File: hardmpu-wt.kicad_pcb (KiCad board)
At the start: 2 copper layers, 106 x 95.3 mm, 49 parts, among them J1 MIDI, J2 User, J3 LineOut, J4 ISP, J5 JTAG, J6 Wavetable, J7 AuxOut, J8 XT Bus, U1 74HCT138, U10 78L05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

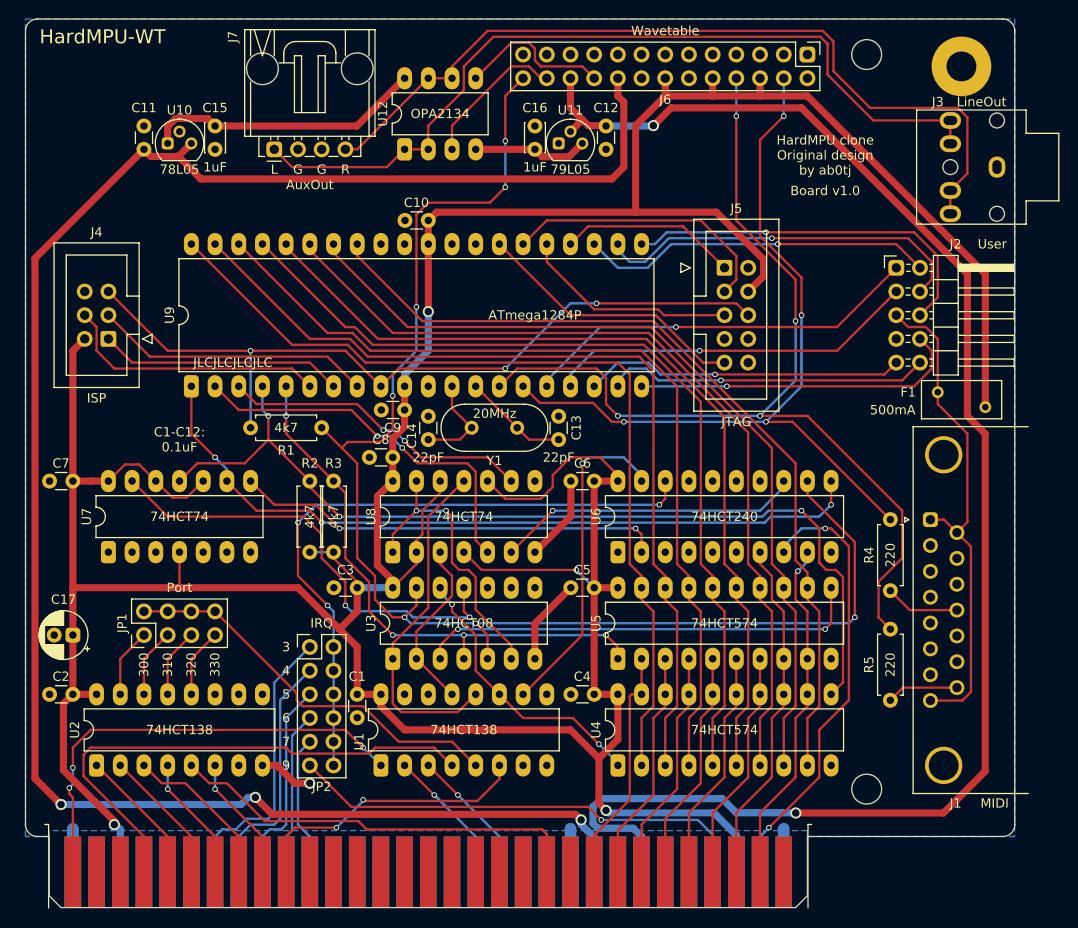
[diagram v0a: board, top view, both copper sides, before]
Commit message: Tweak component values
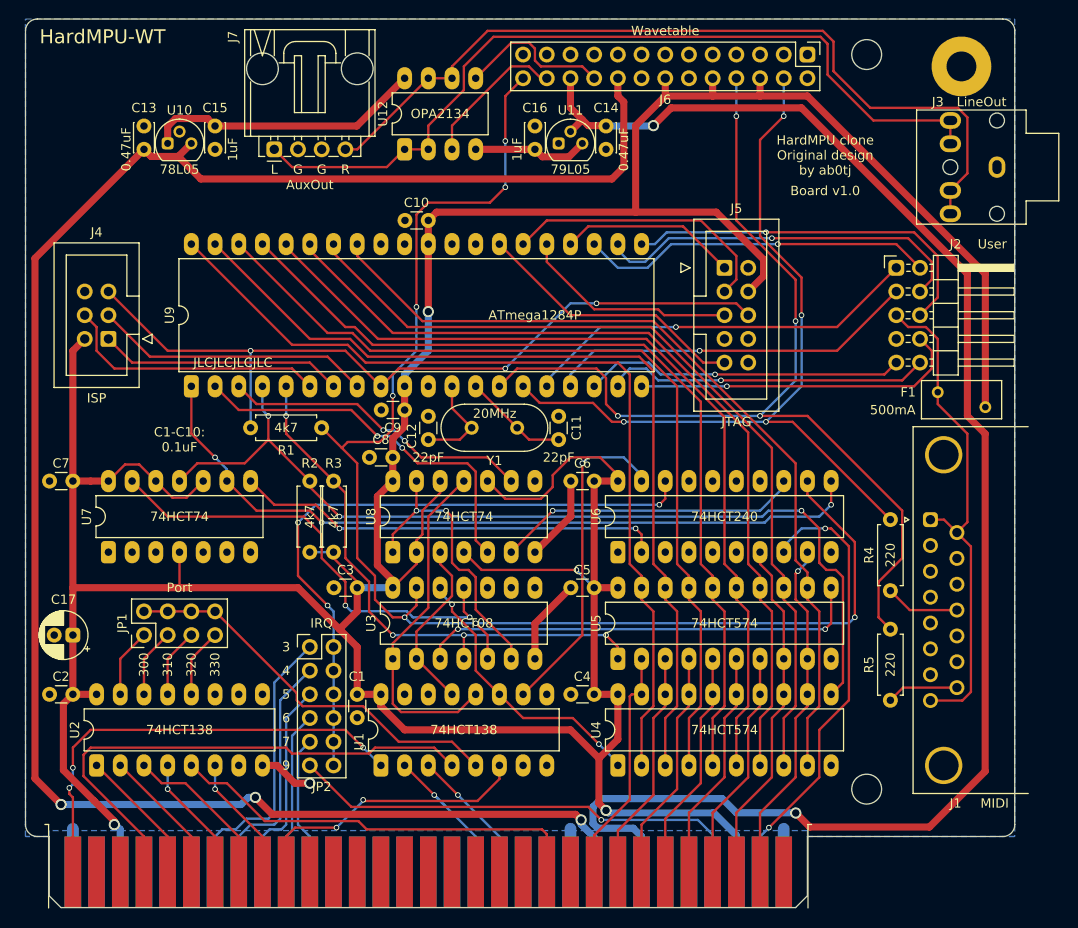
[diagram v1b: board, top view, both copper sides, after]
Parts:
- removed the C11 at (96.5, 67.3)
- removed the C12 at (146.1, 67.3)
- added C13: 0.47uF, Capacitor_THT:C_Disc_D3.0mm_W2.0mm_P2.50mm, F.Cu at (96.5, 67.3)
- added C14: 0.47uF, Capacitor_THT:C_Disc_D3.0mm_W2.0mm_P2.50mm, F.Cu at (146.1, 67.3)
- renumbered C13 to C11, C14 to C12
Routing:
- net -12V: track 166.9 -> 168.1 mm
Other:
- board text added: "C1-C10: 0.1uF"
- board text removed: "C1-C12: 0.1uF"

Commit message: Move DA-15 so board aligns with Keystone 9200-11 bracket
Adapt board to fit common Keystone 9200-11, add jumpers to switch wavetable between Internal and External UART
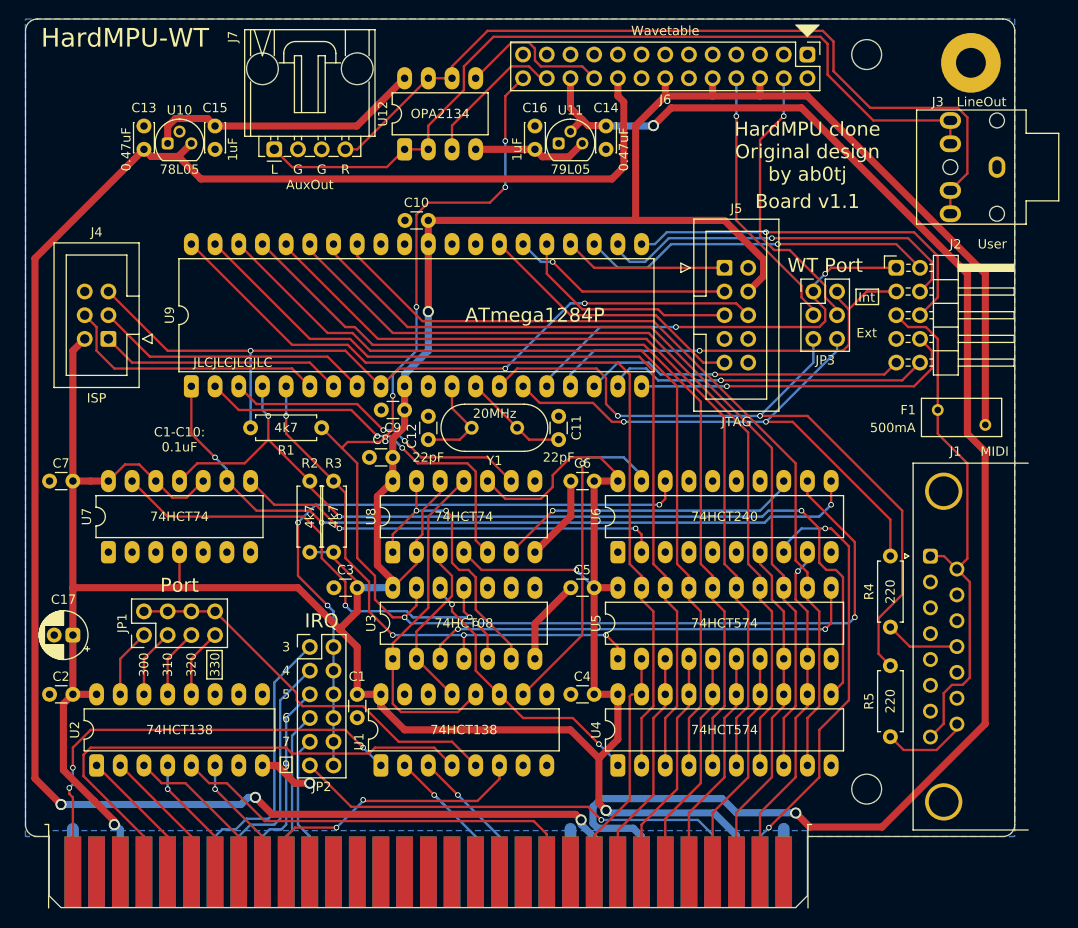
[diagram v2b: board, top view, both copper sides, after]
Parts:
- added JP3: WT Port, Connector_PinHeader_2.54mm:PinHeader_2x03_P2.54mm_Vertical, F.Cu at (168.3, 82.5)
- H1: value WT_Hole1 -> WT_Hole
- H2: value WT_Hole2 -> WT_Hole
- moved J1 3.91 mm to (180.8, 110.9)
- moved R5 3.91 mm to (176.5, 130.3)
- moved R4 3.91 mm to (176.5, 118.5)
- moved F1 1.91 mm to (181.6, 95.2)
- moved H3 1.09 mm to (185.2, 58.0)
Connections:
- J2 pad 1: /USER0 -> /RX1
- J2 pad 10: /USER3 -> /USER1
- J2 pad 3: /USER1 -> /TX1
- J2 pad 6: /USER5 -> /USER3
- J2 pad 8: /USER4 -> /USER2
- J2 pad 9: /USER2 -> /USER0
- J6 pad 4: MIDI_TX -> WT_TX
- J6 pad 8: MIDI_RX -> WT_RX
- R4 pad 2: MIDI_TX -> /TX0
- R5 pad 2: MIDI_RX -> /RX0
- U9 pad 14: MIDI_RX -> /RX0
- U9 pad 15: MIDI_TX -> /TX0
- U9 pad 16: /USER0 -> /RX1
- U9 pad 17: /USER1 -> /TX1
- U9 pad 18: /USER2 -> /USER0
- U9 pad 19: /USER3 -> /USER1
- U9 pad 20: /USER4 -> /USER2
- U9 pad 21: /USER5 -> /USER3
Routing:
- net MIDI_RX: track 106.6 -> 0.00 mm, vias 4 -> 0
- net MIDI_TX: track 86.6 -> 0.00 mm, vias 4 -> 0
- net /RX0: track 0.00 -> 80.7 mm, vias 0 -> 2
- net /TX0: track 0.00 -> 61.2 mm, vias 0 -> 2
- net /RX1: track 0.00 -> 47.1 mm, vias 0 -> 2
- net /TX1: track 0.00 -> 44.5 mm, vias 0 -> 1
- net /USER5: track 40.5 -> 0.00 mm, vias 1 -> 0
- net /USER4: track 35.6 -> 0.00 mm, vias 1 -> 0
- net WT_TX: track 0.00 -> 30.8 mm, vias 0 -> 1
- net WT_RX: track 0.00 -> 28.8 mm, vias 0 -> 1
- net /USER0: track 43.1 -> 34.5 mm
- net /TDO: track 29.8 -> 23.7 mm, vias 0 -> 1
- net /USER3: track 34.9 -> 40.5 mm
- net /USER1: track 39.9 -> 34.9 mm
- net -12V: track 168.1 -> 165.2 mm
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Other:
- board text added: "Board v1.1"
- board text added: "Ext"
- board text added: "Int"
- board text removed: "Board v1.0"

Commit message: Migrate project to KiCad 6
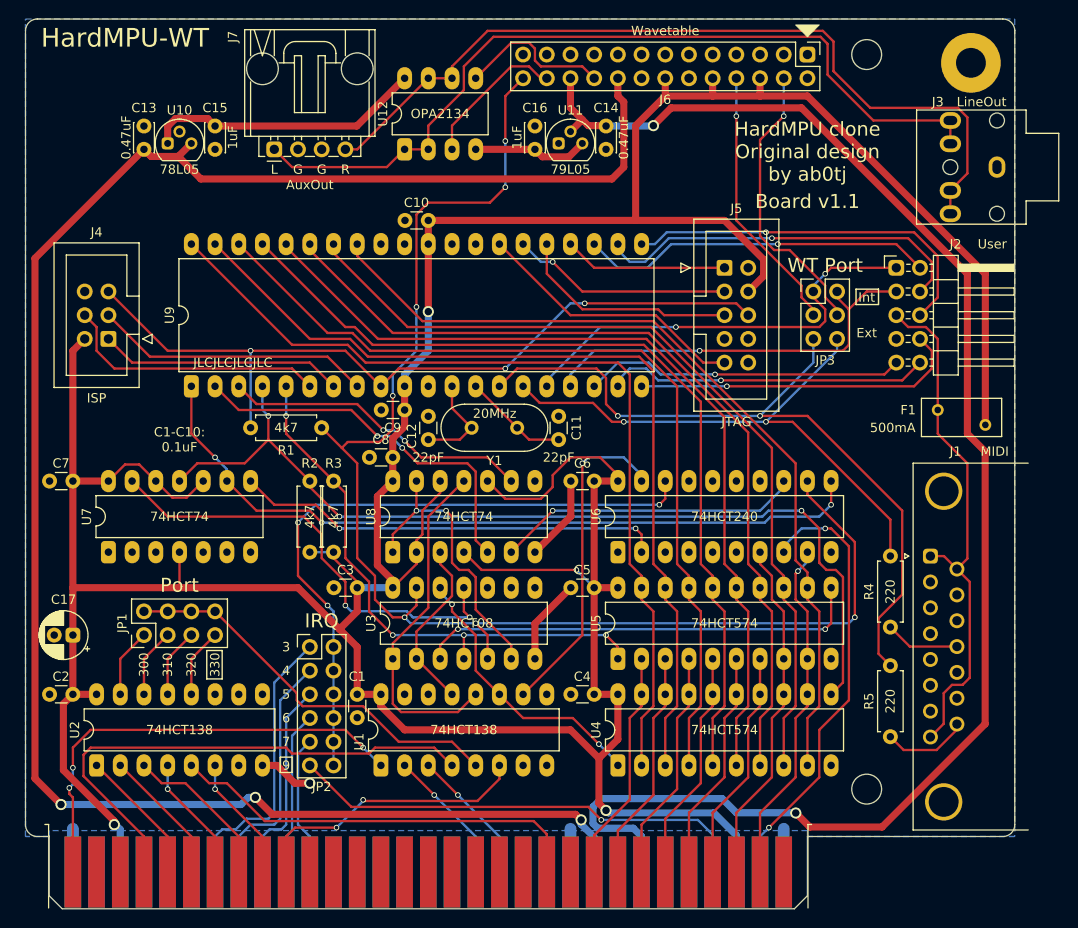
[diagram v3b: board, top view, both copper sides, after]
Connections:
- net /~AVRRST renamed /~{AVRRST}
- net /~CR renamed /~{CR}
- net /~CW renamed /~{CW}
- net /~DR renamed /~{DR}
- net /~DRCLK renamed /~{DRCLK}
- net /~DRR renamed /~{DRR}
- net /~DRRS renamed /~{DRRS}
- net /~DSR renamed /~{DSR}
- net /~DW renamed /~{DW}
- net /~IDR renamed /~{IDR}
- net /~IDRRS renamed /~{IDRRS}
- net /~IDW renamed /~{IDW}
- net /~IOCS renamed /~{IOCS}
- net /~IOR renamed /~{IOR}
- net /~IOW renamed /~{IOW}
- net ~RESET renamed ~{RESET}
- H3 pad 1: Net-(H3-Pad1) -> unconnected-(H3-Pad1)
- J1 pad 10: Net-(J1-Pad10) -> unconnected-(J1-Pad10)
- J1 pad 11: Net-(J1-Pad11) -> unconnected-(J1-Pad11)
- J1 pad 13: Net-(J1-Pad13) -> unconnected-(J1-Pad13)
- J1 pad 14: Net-(J1-Pad14) -> unconnected-(J1-Pad14)
- J1 pad 2: Net-(J1-Pad2) -> unconnected-(J1-Pad2)
- J1 pad 3: Net-(J1-Pad3) -> unconnected-(J1-Pad3)
- J1 pad 6: Net-(J1-Pad6) -> unconnected-(J1-Pad6)
- J1 pad 7: Net-(J1-Pad7) -> unconnected-(J1-Pad7)
- J5 pad 7: Net-(J5-Pad7) -> unconnected-(J5-Pad7)
- J5 pad 8: Net-(J5-Pad8) -> unconnected-(J5-Pad8)
- J6 pad 13: Net-(J6-Pad13) -> unconnected-(J6-Pad13)
- J6 pad 2: Net-(J6-Pad2) -> unconnected-(J6-Pad2)
- J8 pad 11: Net-(J8-Pad11) -> unconnected-(J8-Pad11)
- J8 pad 12: Net-(J8-Pad12) -> unconnected-(J8-Pad12)
- J8 pad 15: Net-(J8-Pad15) -> unconnected-(J8-Pad15)
- J8 pad 16: Net-(J8-Pad16) -> unconnected-(J8-Pad16)
- J8 pad 17: Net-(J8-Pad17) -> unconnected-(J8-Pad17)
- J8 pad 18: Net-(J8-Pad18) -> unconnected-(J8-Pad18)
- J8 pad 19: Net-(J8-Pad19) -> unconnected-(J8-Pad19)
- J8 pad 20: Net-(J8-Pad20) -> unconnected-(J8-Pad20)
- J8 pad 26: Net-(J8-Pad26) -> unconnected-(J8-Pad26)
- J8 pad 27: Net-(J8-Pad27) -> unconnected-(J8-Pad27)
- J8 pad 28: Net-(J8-Pad28) -> unconnected-(J8-Pad28)
- J8 pad 30: Net-(J8-Pad30) -> unconnected-(J8-Pad30)
- J8 pad 32: Net-(J8-Pad32) -> unconnected-(J8-Pad32)
- J8 pad 41: Net-(J8-Pad41) -> unconnected-(J8-Pad41)
- J8 pad 43: Net-(J8-Pad43) -> unconnected-(J8-Pad43)
- J8 pad 44: Net-(J8-Pad44) -> unconnected-(J8-Pad44)
- J8 pad 45: Net-(J8-Pad45) -> unconnected-(J8-Pad45)
- J8 pad 46: Net-(J8-Pad46) -> unconnected-(J8-Pad46)
- J8 pad 47: Net-(J8-Pad47) -> unconnected-(J8-Pad47)
- J8 pad 48: Net-(J8-Pad48) -> unconnected-(J8-Pad48)
- J8 pad 49: Net-(J8-Pad49) -> unconnected-(J8-Pad49)
- J8 pad 5: Net-(J8-Pad5) -> unconnected-(J8-Pad5)
- J8 pad 50: Net-(J8-Pad50) -> unconnected-(J8-Pad50)
- J8 pad 51: Net-(J8-Pad51) -> unconnected-(J8-Pad51)
- J8 pad 52: Net-(J8-Pad52) -> unconnected-(J8-Pad52)
- J8 pad 6: Net-(J8-Pad6) -> unconnected-(J8-Pad6)
- J8 pad 60: Net-(J8-Pad60) -> unconnected-(J8-Pad60)
- J8 pad 61: Net-(J8-Pad61) -> unconnected-(J8-Pad61)
- J8 pad 8: Net-(J8-Pad8) -> unconnected-(J8-Pad8)
- U1 pad 14: Net-(U1-Pad14) -> unconnected-(U1-Pad14)
- U1 pad 15: Net-(U1-Pad15) -> unconnected-(U1-Pad15)
- U1 pad 7: Net-(U1-Pad7) -> unconnected-(U1-Pad7)
- U1 pad 9: Net-(U1-Pad9) -> unconnected-(U1-Pad9)
- U2 pad 10: Net-(U2-Pad10) -> unconnected-(U2-Pad10)
- U2 pad 11: Net-(U2-Pad11) -> unconnected-(U2-Pad11)
- U2 pad 7: Net-(U2-Pad7) -> unconnected-(U2-Pad7)
- U2 pad 9: Net-(U2-Pad9) -> unconnected-(U2-Pad9)
- U3 pad 8: Net-(U3-Pad8) -> unconnected-(U3-Pad8)
- U6 pad 14: Net-(U6-Pad14) -> unconnected-(U6-Pad14)
- U6 pad 16: Net-(U6-Pad16) -> unconnected-(U6-Pad16)
- U6 pad 3: Net-(U6-Pad3) -> unconnected-(U6-Pad3)
- U6 pad 5: Net-(U6-Pad5) -> unconnected-(U6-Pad5)
- U7 pad 5: Net-(U7-Pad5) -> unconnected-(U7-Pad5)
- U7 pad 6: Net-(U7-Pad6) -> unconnected-(U7-Pad6)
- U8 pad 8: Net-(U8-Pad8) -> unconnected-(U8-Pad8)
- U9 pad 28: Net-(U9-Pad28) -> unconnected-(U9-Pad28)
- U9 pad 29: Net-(U9-Pad29) -> unconnected-(U9-Pad29)
- U9 pad 32: Net-(U9-Pad32) -> unconnected-(U9-Pad32)
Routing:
- net /~{IOR}: track 16.4 -> 14.6 mm
- net /IRQ: track 70.6 -> 69.9 mm
- net /DB0: track 25.6 -> 25.0 mm
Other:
- board size 106 x 95.3 mm -> 106 x 95.4 mm
- net class Default removed
- net class Power removed
